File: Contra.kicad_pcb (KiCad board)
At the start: 2 copper layers, 231 x 76.2 mm, 125 parts, among them P1 Pad, P2 Pad, P3 Pad, P4 Pad, SW1 SW_PUSH, U1 ProMicro

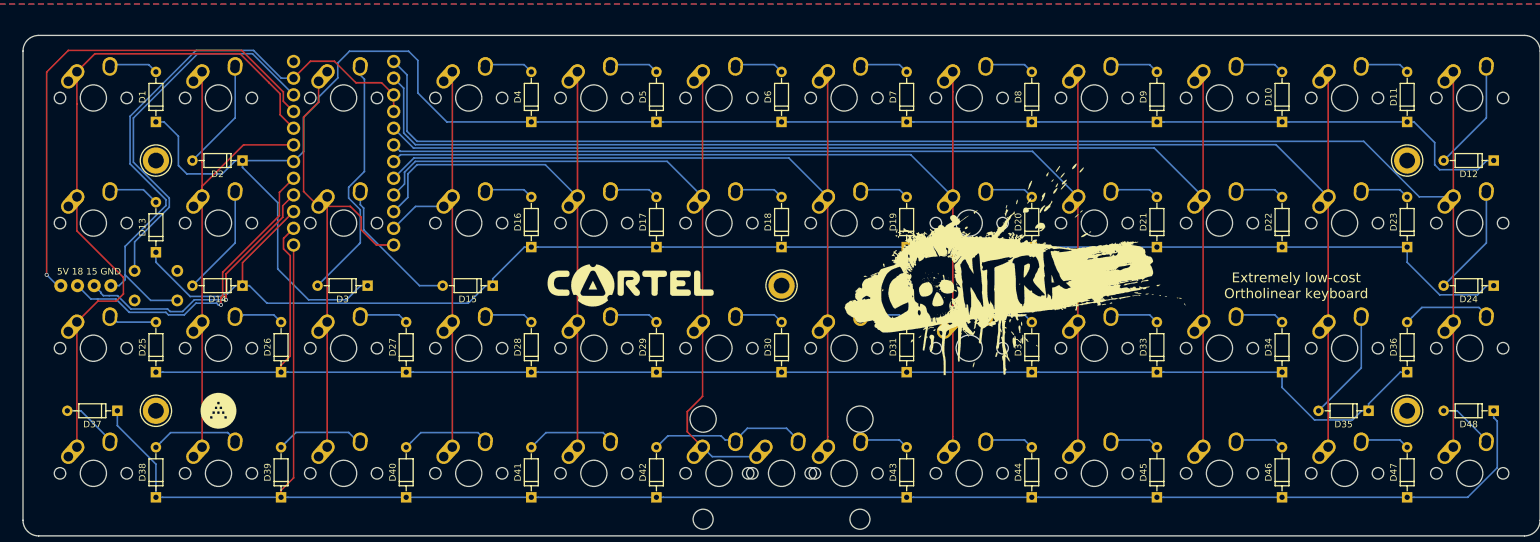
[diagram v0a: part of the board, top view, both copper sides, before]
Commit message: initial commit for wireless mods for BlueMicro
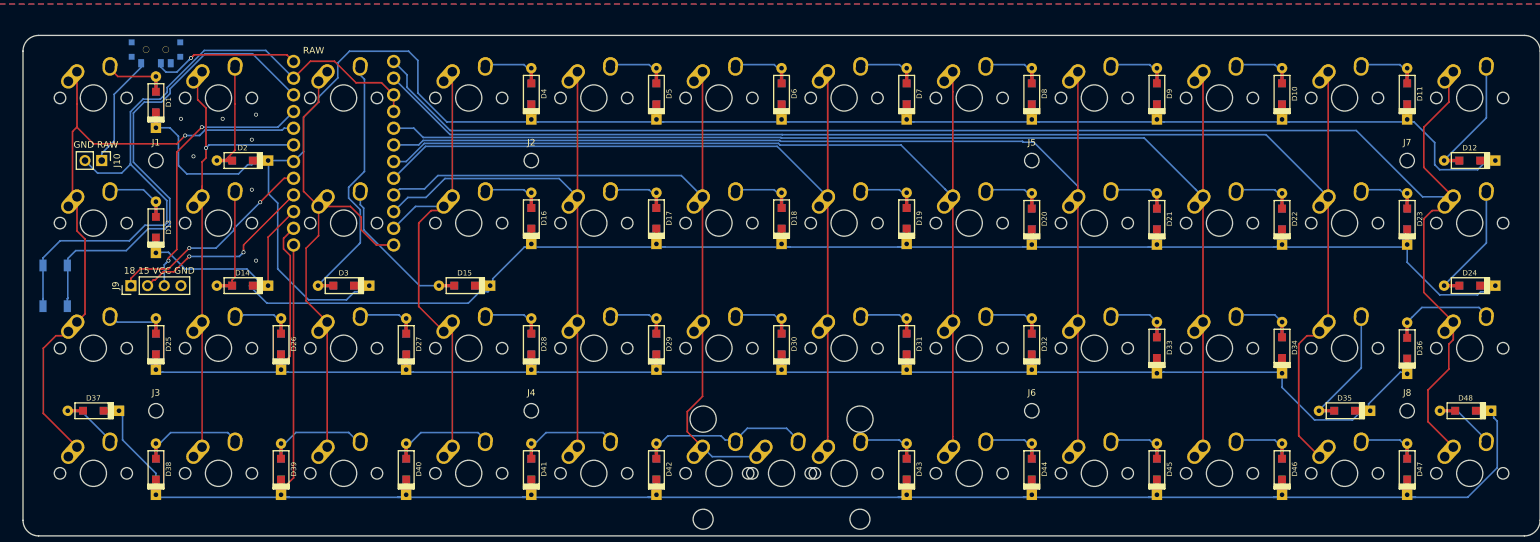
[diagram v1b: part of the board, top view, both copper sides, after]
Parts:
- removed G***: LOGO, memelogo:wey
- removed G***: LOGO, memelogo:boboxsmall
- removed G***: LOGO, memelogo:thonksmall
- removed G***: LOGO, memelogo:cartel
- removed G***: LOGO, memelogo:thinkster
- removed G***: LOGO, memelogo:datboi
- removed G***: LOGO, memelogo:bobbyhill
- removed G***: LOGO, memelogo:dickbutt
- removed G***: LOGO, ai03-logo:AI03-Silkscreen-5.4mm
- removed G***: LOGO, memelogo:broken
- removed G***: LOGO, memelogo:youwat
- removed G***: LOGO, memelogo:dopre
- removed G***: LOGO, memelogo:contra
- removed G***: LOGO, memelogo:magicalleaf
- removed G***: LOGO, memelogo:reeeeeee
- removed G***: LOGO, memelogo:stem
- removed G***: LOGO, memelogo:righthand
- removed P1, P2, P3, P4: Pad, locallib:mountinghole
- removed REF** (x5): mountinghole, locallib:mountinghole
- added J1: Conn_01x01, MountingHole:MountingHole_2.2mm_M2_ISO7380, F.Cu at (47.6, 47.6)
- added J10: Conn_01x02, Connector_PinHeader_2.54mm:PinHeader_1x02_P2.54mm_Vertical, F.Cu at (39.4, 47.6)
- added J2: Conn_01x01, MountingHole:MountingHole_2.2mm_M2_ISO7380, F.Cu at (104.8, 47.6)
- added J3: Conn_01x01, MountingHole:MountingHole_2.2mm_M2_ISO7380, F.Cu at (47.6, 85.7)
- added J4: Conn_01x01, MountingHole:MountingHole_2.2mm_M2_ISO7380, F.Cu at (104.8, 85.7)
- added J5: Conn_01x01, MountingHole:MountingHole_2.2mm_M2_ISO7380, F.Cu at (181.0, 47.6)
- added J6: Conn_01x01, MountingHole:MountingHole_2.2mm_M2_ISO7380, F.Cu at (181.0, 85.7)
- added J7: Conn_01x01, MountingHole:MountingHole_2.2mm_M2_ISO7380, F.Cu at (238.1, 47.6)
- added J8: Conn_01x01, MountingHole:MountingHole_2.2mm_M2_ISO7380, F.Cu at (238.1, 85.7)
- added J9: Conn_01x04, Connector_PinHeader_2.54mm:PinHeader_1x04_P2.54mm_Vertical, F.Cu at (43.8, 66.7)
- added SW2: SW_SPDT, footprints:SPDT_C128955, B.Cu at (47.6, 30.7)
- D1, D10, D11, D12, D13, D14, D15, D16, D17, D18, D19, D2, D20, D21, D22, D23, D24, D25, D26, D27, D28, D29, D3, D30, D31, D32, D33, D34, D35, D36, D37, D38, D39, D4, D40, D41, D42, D43, D44, D45, D46, D47, D48, D5, D6, D7, D8, D9: footprint Diodes_THT:D_DO-35_SOD27_P7.62mm_Horizontal -> footprints:D_SOD123_axial-dual
- SW1: footprint Molex-0548190589:PushButton_6x6mm_TH -> footprints:SW_TACT_ALPS_SKQGABE010
- moved SW1 15.3 mm to (32.3, 66.7), turned to 90 degrees
- moved D16 4.38 mm to (104.8, 56.4)
- moved D17 4.38 mm to (123.8, 56.4)
- moved D18 4.38 mm to (142.9, 56.4)
- moved D19 4.38 mm to (161.9, 56.4)
- moved D48 4.29 mm to (247.0, 85.7)
- moved D15 4.29 mm to (94.6, 66.7)
- moved D38 4.29 mm to (47.6, 94.6)
- moved D39 4.29 mm to (66.7, 94.6)
- moved D40 4.29 mm to (85.7, 94.6)
- moved D41 4.29 mm to (104.8, 94.6)
- moved D42 4.29 mm to (123.8, 94.6)
- moved D43 4.29 mm to (161.9, 94.6)
- moved D44 4.29 mm to (181.0, 94.6)
- moved D45 4.29 mm to (200.0, 94.6)
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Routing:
- net +5V: track 77.4 -> 41.5 mm, vias 1 -> 2
- net Net-(SW2-Pad2): track 0.00 -> 22.9 mm, vias 0 -> 1
- net ROW3: track 269.8 -> 291.3 mm
- net Net-(J10-Pad1): track 0.00 -> 17.6 mm
- net Net-(SW1-Pad1): track 58.8 -> 75.4 mm
- net Net-(J9-Pad1): track 48.4 -> 32.3 mm, vias 1 -> 2
- net GND: track 93.6 -> 107.7 mm, vias 0 -> 7
- net Net-(J9-Pad2): track 42.7 -> 28.6 mm, vias 1 -> 2
- net ROW1: track 232.7 -> 246.7 mm
- net COL11: track 232.1 -> 239.4 mm
- net COL0: track 105.3 -> 98.6 mm, vias 0 -> 1
- net COL4: track 93.9 -> 90.1 mm
- net COL3: track 67.5 -> 71.3 mm
- net Net-(D14-Pad2): track 17.3 -> 14.2 mm
- net COL5: track 120.3 -> 117.5 mm
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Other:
- board text added: "18 15 VCC GND"
- board text added: "GND RAW"
- board text added: "RAW"
- board text removed: "+5V"
- board text removed: "5V 18 15 GND"
- board text removed: "CAUTION: Toxic Memes. DO NOT EAT. Do not wash with beer."
- board text removed: "CONTRA"
- board text removed: "Extremely low-cost Ortholinear keyboard"
- board text removed: "Pro Micro here! Component side faces away from the PCB. Rev 1.6"
- board text removed: "criminally cheap ortho"
